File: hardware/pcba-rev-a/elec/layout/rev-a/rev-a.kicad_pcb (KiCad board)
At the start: 4 copper layers, 160 x 100 mm, 0 parts

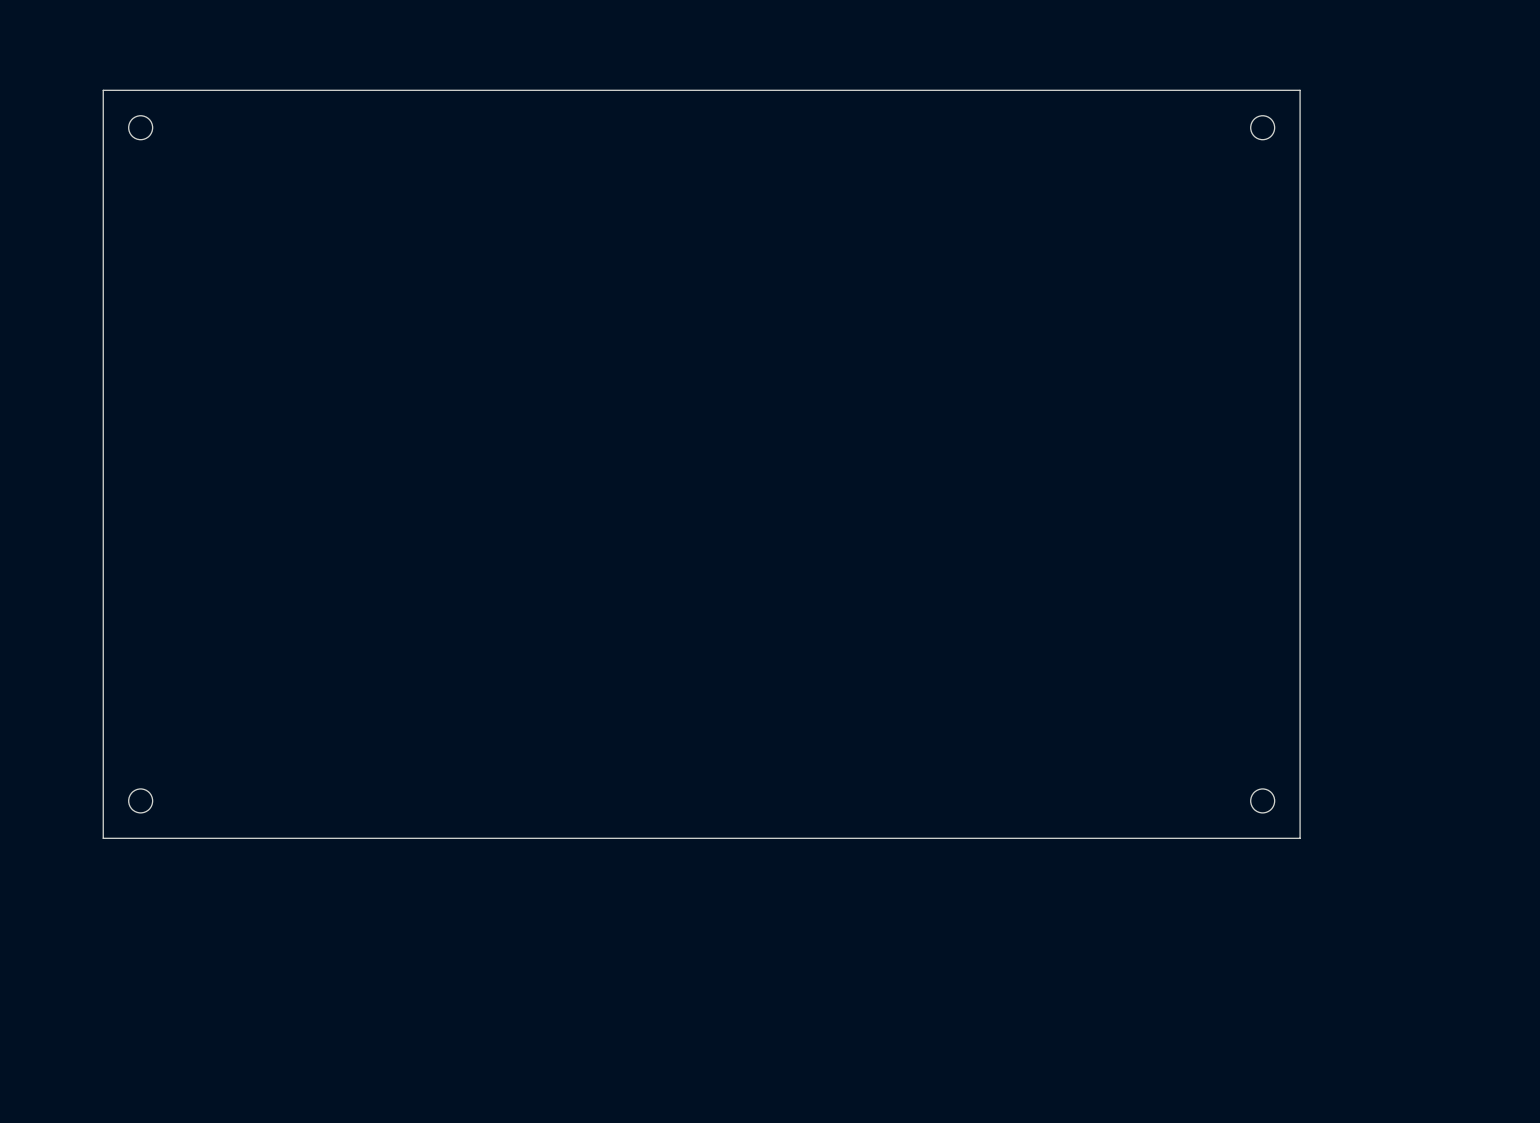
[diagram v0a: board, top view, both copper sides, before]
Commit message: Rev A board populated: 154 components, 55 nets, floorplan placement
scripts/gen_board.py generates the .kicad_pcb directly from the design
structure: 8 lane-selector trees (64 G6K-2F-Y + 24 reed SIP), 8x
protection channels (PTC/steering/TVS/comparator), 12x TPIC6B595 coil
sink chain + power tree on the north strip, socketed Pico 2 module +
watchdog + cal EEPROM south, reference block reeds on the analog
island, J10 SEAF west, instrument connectors east. Real net structure
(lane buses, bank nets, probe tips/nodes, coil/control rails) so the
ratsnest shows the architecture in pcbnew. Reconciles against the
atopile netlist when the 0.15 migration lands.

Co-Authored-By: Claude Fable 5 <noreply@anthropic.com>
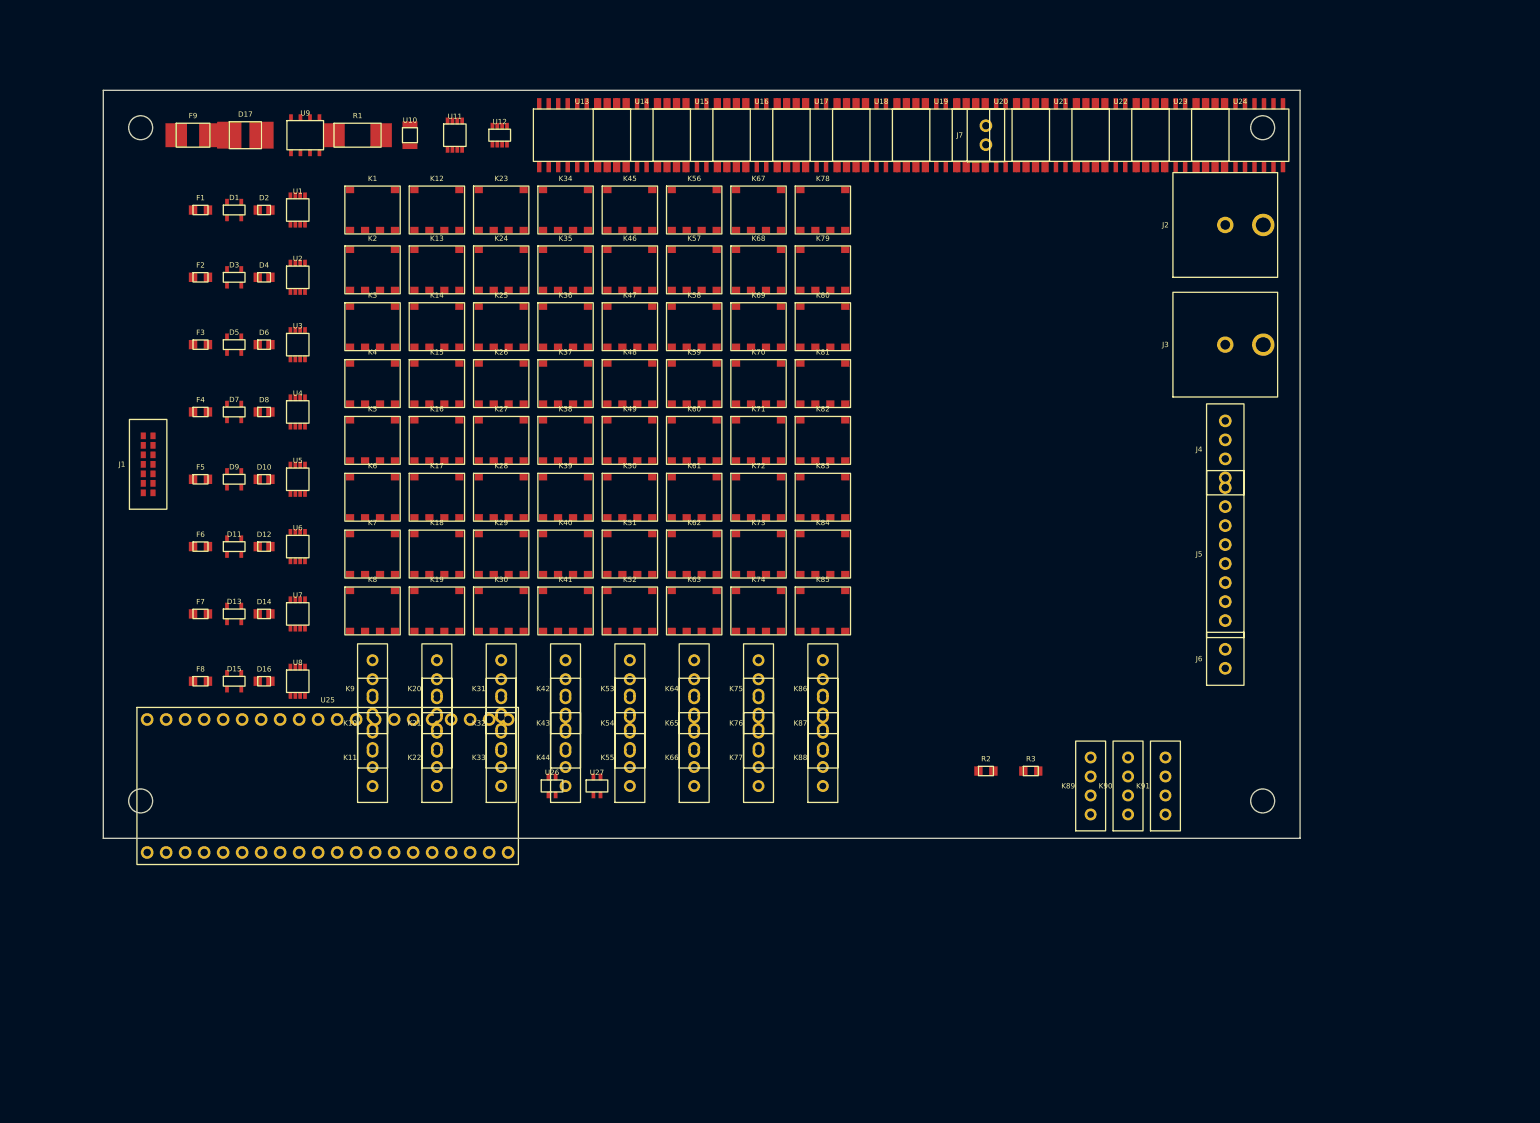
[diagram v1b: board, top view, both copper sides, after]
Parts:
- added D1: , EE:SOT23, F.Cu at (67.5, 66.0)
- added D10: , EE:SOD323, F.Cu at (71.5, 102.0)
- added D11: , EE:SOT23, F.Cu at (67.5, 111.0)
- added D12: , EE:SOD323, F.Cu at (71.5, 111.0)
- added D13: , EE:SOT23, F.Cu at (67.5, 120.0)
- added D14: , EE:SOD323, F.Cu at (71.5, 120.0)
- added D15: , EE:SOT23, F.Cu at (67.5, 129.0)
- added D16: , EE:SOD323, F.Cu at (71.5, 129.0)
- added D17: , EE:SMB, F.Cu at (69.0, 56.0)
- added D2: , EE:SOD323, F.Cu at (71.5, 66.0)
- added D3: , EE:SOT23, F.Cu at (67.5, 75.0)
- added D4: , EE:SOD323, F.Cu at (71.5, 75.0)
- added D5: , EE:SOT23, F.Cu at (67.5, 84.0)
- added D6: , EE:SOD323, F.Cu at (71.5, 84.0)
- added D7: , EE:SOT23, F.Cu at (67.5, 93.0)
- added D8: , EE:SOD323, F.Cu at (71.5, 93.0)
- added D9: , EE:SOT23, F.Cu at (67.5, 102.0)
- added F1: , EE:PTC0805, F.Cu at (63.0, 66.0)
- added F2: , EE:PTC0805, F.Cu at (63.0, 75.0)
- added F3: , EE:PTC0805, F.Cu at (63.0, 84.0)
- added F4: , EE:PTC0805, F.Cu at (63.0, 93.0)
- added F5: , EE:PTC0805, F.Cu at (63.0, 102.0)
- added F6: , EE:PTC0805, F.Cu at (63.0, 111.0)
- added F7: , EE:PTC0805, F.Cu at (63.0, 120.0)
- added F8: , EE:PTC0805, F.Cu at (63.0, 129.0)
- added F9: , EE:FUSE1812, F.Cu at (62.0, 56.0)
- added J1: , EE:SEAF14, F.Cu at (56.0, 100.0)
- added J2: , EE:BNC_TH, F.Cu at (200.0, 68.0)
- added J3: , EE:BNC_TH, F.Cu at (200.0, 84.0)
- added J4: , EE:HDR4, F.Cu at (200.0, 98.0)
- added J5: , EE:HDR8, F.Cu at (200.0, 112.0)
- added J6: , EE:HDR2, F.Cu at (200.0, 126.0)
- added J7: , EE:HDR2, F.Cu at (168.0, 56.0)
- added K1: , EE:RELAY_G6K2FY, F.Cu at (86.0, 66.0)
- added K10: , EE:REED_SIP4, F.Cu at (86.0, 134.6)
- added K11: , EE:REED_SIP4, F.Cu at (86.0, 139.2)
- added K12: , EE:RELAY_G6K2FY, F.Cu at (94.6, 66.0)
- added K13: , EE:RELAY_G6K2FY, F.Cu at (94.6, 74.0)
- added K14: , EE:RELAY_G6K2FY, F.Cu at (94.6, 81.6)
- added K15: , EE:RELAY_G6K2FY, F.Cu at (94.6, 89.2)
- added K16: , EE:RELAY_G6K2FY, F.Cu at (94.6, 96.8)
- added K17: , EE:RELAY_G6K2FY, F.Cu at (94.6, 104.4)
- added K18: , EE:RELAY_G6K2FY, F.Cu at (94.6, 112.0)
- added K19: , EE:RELAY_G6K2FY, F.Cu at (94.6, 119.6)
- added K2: , EE:RELAY_G6K2FY, F.Cu at (86.0, 74.0)
- added K20: , EE:REED_SIP4, F.Cu at (94.6, 130.0)
- added K21: , EE:REED_SIP4, F.Cu at (94.6, 134.6)
- added K22: , EE:REED_SIP4, F.Cu at (94.6, 139.2)
- added K23: , EE:RELAY_G6K2FY, F.Cu at (103.2, 66.0)
- added K24: , EE:RELAY_G6K2FY, F.Cu at (103.2, 74.0)
- added K25: , EE:RELAY_G6K2FY, F.Cu at (103.2, 81.6)
- added K26: , EE:RELAY_G6K2FY, F.Cu at (103.2, 89.2)
- added K27: , EE:RELAY_G6K2FY, F.Cu at (103.2, 96.8)
- added K28: , EE:RELAY_G6K2FY, F.Cu at (103.2, 104.4)
- added K29: , EE:RELAY_G6K2FY, F.Cu at (103.2, 112.0)
- added K3: , EE:RELAY_G6K2FY, F.Cu at (86.0, 81.6)
- added K30: , EE:RELAY_G6K2FY, F.Cu at (103.2, 119.6)
- added K31: , EE:REED_SIP4, F.Cu at (103.2, 130.0)
- added K32: , EE:REED_SIP4, F.Cu at (103.2, 134.6)
- added K33: , EE:REED_SIP4, F.Cu at (103.2, 139.2)
- added K34: , EE:RELAY_G6K2FY, F.Cu at (111.8, 66.0)
- added K35: , EE:RELAY_G6K2FY, F.Cu at (111.8, 74.0)
- added K36: , EE:RELAY_G6K2FY, F.Cu at (111.8, 81.6)
- added K37: , EE:RELAY_G6K2FY, F.Cu at (111.8, 89.2)
- added K38: , EE:RELAY_G6K2FY, F.Cu at (111.8, 96.8)
- added K39: , EE:RELAY_G6K2FY, F.Cu at (111.8, 104.4)
- added K4: , EE:RELAY_G6K2FY, F.Cu at (86.0, 89.2)
- added K40: , EE:RELAY_G6K2FY, F.Cu at (111.8, 112.0)
- added K41: , EE:RELAY_G6K2FY, F.Cu at (111.8, 119.6)
- added K42: , EE:REED_SIP4, F.Cu at (111.8, 130.0)
- added K43: , EE:REED_SIP4, F.Cu at (111.8, 134.6)
- added K44: , EE:REED_SIP4, F.Cu at (111.8, 139.2)
- added K45: , EE:RELAY_G6K2FY, F.Cu at (120.4, 66.0)
- added K46: , EE:RELAY_G6K2FY, F.Cu at (120.4, 74.0)
- added K47: , EE:RELAY_G6K2FY, F.Cu at (120.4, 81.6)
- added K48: , EE:RELAY_G6K2FY, F.Cu at (120.4, 89.2)
- added K49: , EE:RELAY_G6K2FY, F.Cu at (120.4, 96.8)
- added K5: , EE:RELAY_G6K2FY, F.Cu at (86.0, 96.8)
- added K50: , EE:RELAY_G6K2FY, F.Cu at (120.4, 104.4)
- added K51: , EE:RELAY_G6K2FY, F.Cu at (120.4, 112.0)
- added K52: , EE:RELAY_G6K2FY, F.Cu at (120.4, 119.6)
- added K53: , EE:REED_SIP4, F.Cu at (120.4, 130.0)
- added K54: , EE:REED_SIP4, F.Cu at (120.4, 134.6)
- added K55: , EE:REED_SIP4, F.Cu at (120.4, 139.2)
- added K56: , EE:RELAY_G6K2FY, F.Cu at (129.0, 66.0)
- added K57: , EE:RELAY_G6K2FY, F.Cu at (129.0, 74.0)
- added K58: , EE:RELAY_G6K2FY, F.Cu at (129.0, 81.6)
- added K59: , EE:RELAY_G6K2FY, F.Cu at (129.0, 89.2)
- added K6: , EE:RELAY_G6K2FY, F.Cu at (86.0, 104.4)
- added K60: , EE:RELAY_G6K2FY, F.Cu at (129.0, 96.8)
- added K61: , EE:RELAY_G6K2FY, F.Cu at (129.0, 104.4)
- added K62: , EE:RELAY_G6K2FY, F.Cu at (129.0, 112.0)
- added K63: , EE:RELAY_G6K2FY, F.Cu at (129.0, 119.6)
- added K64: , EE:REED_SIP4, F.Cu at (129.0, 130.0)
- added K65: , EE:REED_SIP4, F.Cu at (129.0, 134.6)
- added K66: , EE:REED_SIP4, F.Cu at (129.0, 139.2)
- added K67: , EE:RELAY_G6K2FY, F.Cu at (137.6, 66.0)
- added K68: , EE:RELAY_G6K2FY, F.Cu at (137.6, 74.0)
- added K69: , EE:RELAY_G6K2FY, F.Cu at (137.6, 81.6)
- added K7: , EE:RELAY_G6K2FY, F.Cu at (86.0, 112.0)
- added K70: , EE:RELAY_G6K2FY, F.Cu at (137.6, 89.2)
- added K71: , EE:RELAY_G6K2FY, F.Cu at (137.6, 96.8)
- added K72: , EE:RELAY_G6K2FY, F.Cu at (137.6, 104.4)
- added K73: , EE:RELAY_G6K2FY, F.Cu at (137.6, 112.0)
- added K74: , EE:RELAY_G6K2FY, F.Cu at (137.6, 119.6)
- added K75: , EE:REED_SIP4, F.Cu at (137.6, 130.0)
- added K76: , EE:REED_SIP4, F.Cu at (137.6, 134.6)
- added K77: , EE:REED_SIP4, F.Cu at (137.6, 139.2)
- added K78: , EE:RELAY_G6K2FY, F.Cu at (146.2, 66.0)
- added K79: , EE:RELAY_G6K2FY, F.Cu at (146.2, 74.0)
- added K8: , EE:RELAY_G6K2FY, F.Cu at (86.0, 119.6)
- added K80: , EE:RELAY_G6K2FY, F.Cu at (146.2, 81.6)
- added K81: , EE:RELAY_G6K2FY, F.Cu at (146.2, 89.2)
- added K82: , EE:RELAY_G6K2FY, F.Cu at (146.2, 96.8)
- added K83: , EE:RELAY_G6K2FY, F.Cu at (146.2, 104.4)
- added K84: , EE:RELAY_G6K2FY, F.Cu at (146.2, 112.0)
- added K85: , EE:RELAY_G6K2FY, F.Cu at (146.2, 119.6)
- added K86: , EE:REED_SIP4, F.Cu at (146.2, 130.0)
- added K87: , EE:REED_SIP4, F.Cu at (146.2, 134.6)
- added K88: , EE:REED_SIP4, F.Cu at (146.2, 139.2)
- added K89: , EE:REED_SIP4, F.Cu at (182.0, 143.0)
- added K9: , EE:REED_SIP4, F.Cu at (86.0, 130.0)
- added K90: , EE:REED_SIP4, F.Cu at (187.0, 143.0)
- added K91: , EE:REED_SIP4, F.Cu at (192.0, 143.0)
- added R1: , EE:R2512, F.Cu at (84.0, 56.0)
- added R2: , EE:R0805, F.Cu at (168.0, 141.0)
- added R3: , EE:R0805, F.Cu at (174.0, 141.0)
- added U1: , EE:MSOP8, F.Cu at (76.0, 66.0)
- added U10: , EE:SON8, F.Cu at (91.0, 56.0)
- added U11: , EE:MSOP8, F.Cu at (97.0, 56.0)
- added U12: , EE:SOT23_8, F.Cu at (103.0, 56.0)
- added U13: , EE:SOIC20W, F.Cu at (114.0, 56.0)
- added U14: , EE:SOIC20W, F.Cu at (122.0, 56.0)
- added U15: , EE:SOIC20W, F.Cu at (130.0, 56.0)
- added U16: , EE:SOIC20W, F.Cu at (138.0, 56.0)
- added U17: , EE:SOIC20W, F.Cu at (146.0, 56.0)
- added U18: , EE:SOIC20W, F.Cu at (154.0, 56.0)
- added U19: , EE:SOIC20W, F.Cu at (162.0, 56.0)
- added U2: , EE:MSOP8, F.Cu at (76.0, 75.0)
- added U20: , EE:SOIC20W, F.Cu at (170.0, 56.0)
- added U21: , EE:SOIC20W, F.Cu at (178.0, 56.0)
- added U22: , EE:SOIC20W, F.Cu at (186.0, 56.0)
- added U23: , EE:SOIC20W, F.Cu at (194.0, 56.0)
- added U24: , EE:SOIC20W, F.Cu at (202.0, 56.0)
- added U25: , EE:PICO2_MODULE, F.Cu at (80.0, 143.0)
- added U26: , EE:SOT23_5W, F.Cu at (110.0, 143.0)
- added U27: , EE:SOT23_5E, F.Cu at (116.0, 143.0)
- added U3: , EE:MSOP8, F.Cu at (76.0, 84.0)
- added U4: , EE:MSOP8, F.Cu at (76.0, 93.0)
- added U5: , EE:MSOP8, F.Cu at (76.0, 102.0)
- added U6: , EE:MSOP8, F.Cu at (76.0, 111.0)
- added U7: , EE:MSOP8, F.Cu at (76.0, 120.0)
- added U8: , EE:MSOP8, F.Cu at (76.0, 129.0)
- added U9: , EE:SOIC8_BUCK, F.Cu at (77.0, 56.0)
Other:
- board text added: "ANALOG ISLAND - moat, guard DMM_HI/LO"
- board text added: "FIRSTLIGHT FL-1 - RELAY/PROBE MATRIX REV A - FLOORPLAN"
- board text removed: "160 x 100 mm, 4-layer: Sig / GND / PWR / Sig"
- board text removed: "8x LANE SELECTOR TREES 88 relays lane buses run east"
- board text removed: "ANALOG ISLAND: reeds + ref block + guard"
- board text removed: "FIRSTLIGHT FL-1 - RELAY/PROBE MATRIX REV A"
- board text removed: "Footprints arrive via atopile netlist sync (ato build) - see README gaps"
- board text removed: "INSTRUMENT CONNECTORS J20-J24 on east edge"
- board text removed: "J10 CARTRIDGE + 8x PROTECTION"
- board text removed: "MOAT: no digital/coil copper guard ring DMM_HI/DMM_LO"
- board text removed: "NORTH: J2 24V IN - POWER TREE - 12x TPIC6B595 COIL SINKS"
- board text removed: "SOUTH-WEST: PICO 2 MODULE + USB"
